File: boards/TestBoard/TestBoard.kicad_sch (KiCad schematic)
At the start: 19 parts, among them J1 Conn_01x04, J2 Conn_01x04, J3 Conn_01x80, J4 Conn_01x13, U1 MCP23017_ML, U2 MCP23017_ML, U3 MCP23017_ML, U4 MCP23017_ML, U5 MCP23017_ML

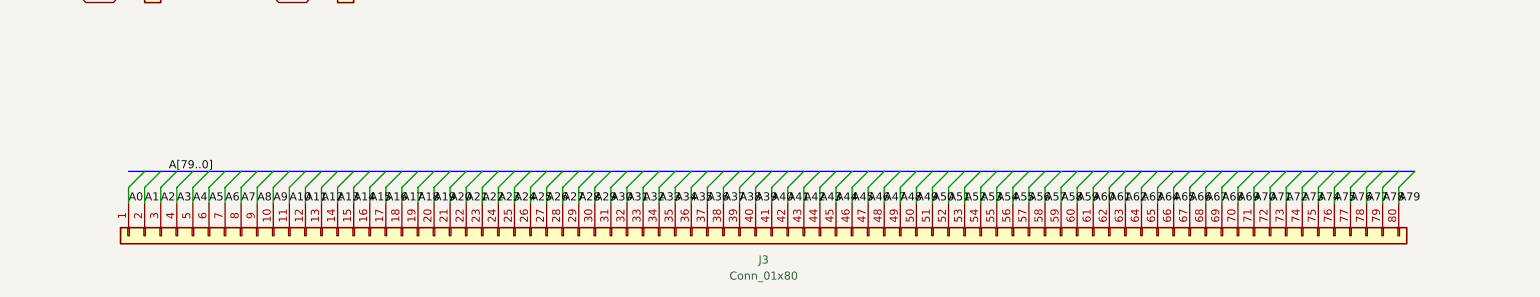
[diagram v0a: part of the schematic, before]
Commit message: Pass-through connectors. Partial manual routing.
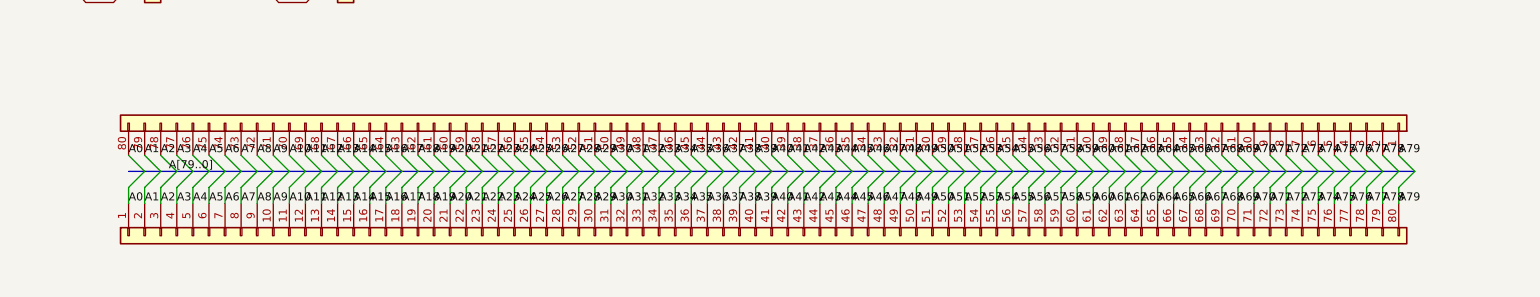
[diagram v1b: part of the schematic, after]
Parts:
- added J5: Conn_01x80, Connector_FFC-FPC:FPC-SMD_THD0518-80CL-GF, symbol Connectors:Conn_01x80
- J4: footprint Connector_PinHeader_2.54mm:PinHeader_1x11_P2.54mm_Vertical -> Connector_PinHeader_2.54mm:PinHeader_1x13_P2.54mm_Vertical
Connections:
- net A0: now also J5.80 (Pin_80)
- net A1: now also J5.79 (Pin_79)
- net A10: now also J5.70 (Pin_70)
- net A11: now also J5.69 (Pin_69)
- net A12: now also J5.68 (Pin_68)
- net A13: now also J5.67 (Pin_67)
- net A14: now also J5.66 (Pin_66)
- net A15: now also J5.65 (Pin_65)
- net A16: now also J5.64 (Pin_64)
- net A17: now also J5.63 (Pin_63)
- net A18: now also J5.62 (Pin_62)
- net A19: now also J5.61 (Pin_61)
- net A2: now also J5.78 (Pin_78)
- net A20: now also J5.60 (Pin_60)
- net A21: now also J5.59 (Pin_59)
- net A22: now also J5.58 (Pin_58)
- net A23: now also J5.57 (Pin_57)
- net A24: now also J5.56 (Pin_56)
- net A25: now also J5.55 (Pin_55)
- net A26: now also J5.54 (Pin_54)
- net A27: now also J5.53 (Pin_53)
- net A28: now also J5.52 (Pin_52)
- net A29: now also J5.51 (Pin_51)
- net A3: now also J5.77 (Pin_77)
- net A30: now also J5.50 (Pin_50)
- net A31: now also J5.49 (Pin_49)
- net A32: now also J5.48 (Pin_48)
- net A33: now also J5.47 (Pin_47)
- net A34: now also J5.46 (Pin_46)
- net A35: now also J5.45 (Pin_45)
- net A36: now also J5.44 (Pin_44)
- net A37: now also J5.43 (Pin_43)
- net A38: now also J5.42 (Pin_42)
- net A39: now also J5.41 (Pin_41)
- net A4: now also J5.76 (Pin_76)
- net A40: now also J5.40 (Pin_40)
- net A41: now also J5.39 (Pin_39)
- net A42: now also J5.38 (Pin_38)
- net A43: now also J5.37 (Pin_37)
- net A44: now also J5.36 (Pin_36)
- net A45: now also J5.35 (Pin_35)
- net A46: now also J5.34 (Pin_34)
- net A47: now also J5.33 (Pin_33)
- net A48: now also J5.32 (Pin_32)
- net A49: now also J5.31 (Pin_31)
- net A5: now also J5.75 (Pin_75)
- net A50: now also J5.30 (Pin_30)
- net A51: now also J5.29 (Pin_29)
- net A52: now also J5.28 (Pin_28)
- net A53: now also J5.27 (Pin_27)
- net A54: now also J5.26 (Pin_26)
- net A55: now also J5.25 (Pin_25)
- net A56: now also J5.24 (Pin_24)
- net A57: now also J5.23 (Pin_23)
- net A58: now also J5.22 (Pin_22)
- net A59: now also J5.21 (Pin_21)
- net A6: now also J5.74 (Pin_74)
- net A60: now also J5.20 (Pin_20)
- net A61: now also J5.19 (Pin_19)
- net A62: now also J5.18 (Pin_18)
- net A63: now also J5.17 (Pin_17)
- net A64: now also J5.16 (Pin_16)
- net A65: now also J5.15 (Pin_15)
- net A66: now also J5.14 (Pin_14)
- net A67: now also J5.13 (Pin_13)
- net A68: now also J5.12 (Pin_12)
- net A69: now also J5.11 (Pin_11)
- net A7: now also J5.73 (Pin_73)
- net A70: now also J5.10 (Pin_10)
- net A71: now also J5.9 (Pin_9)
- net A72: now also J5.8 (Pin_8)
- net A73: now also J5.7 (Pin_7)
- net A74: now also J5.6 (Pin_6)
- net A75: now also J5.5 (Pin_5)
- net A76: now also J5.4 (Pin_4)
- net A77: now also J5.3 (Pin_3)
- net A78: now also J5.2 (Pin_2)
- net A79: now also J5.1 (Pin_1)
- net A8: now also J5.72 (Pin_72)
- net A9: now also J5.71 (Pin_71)

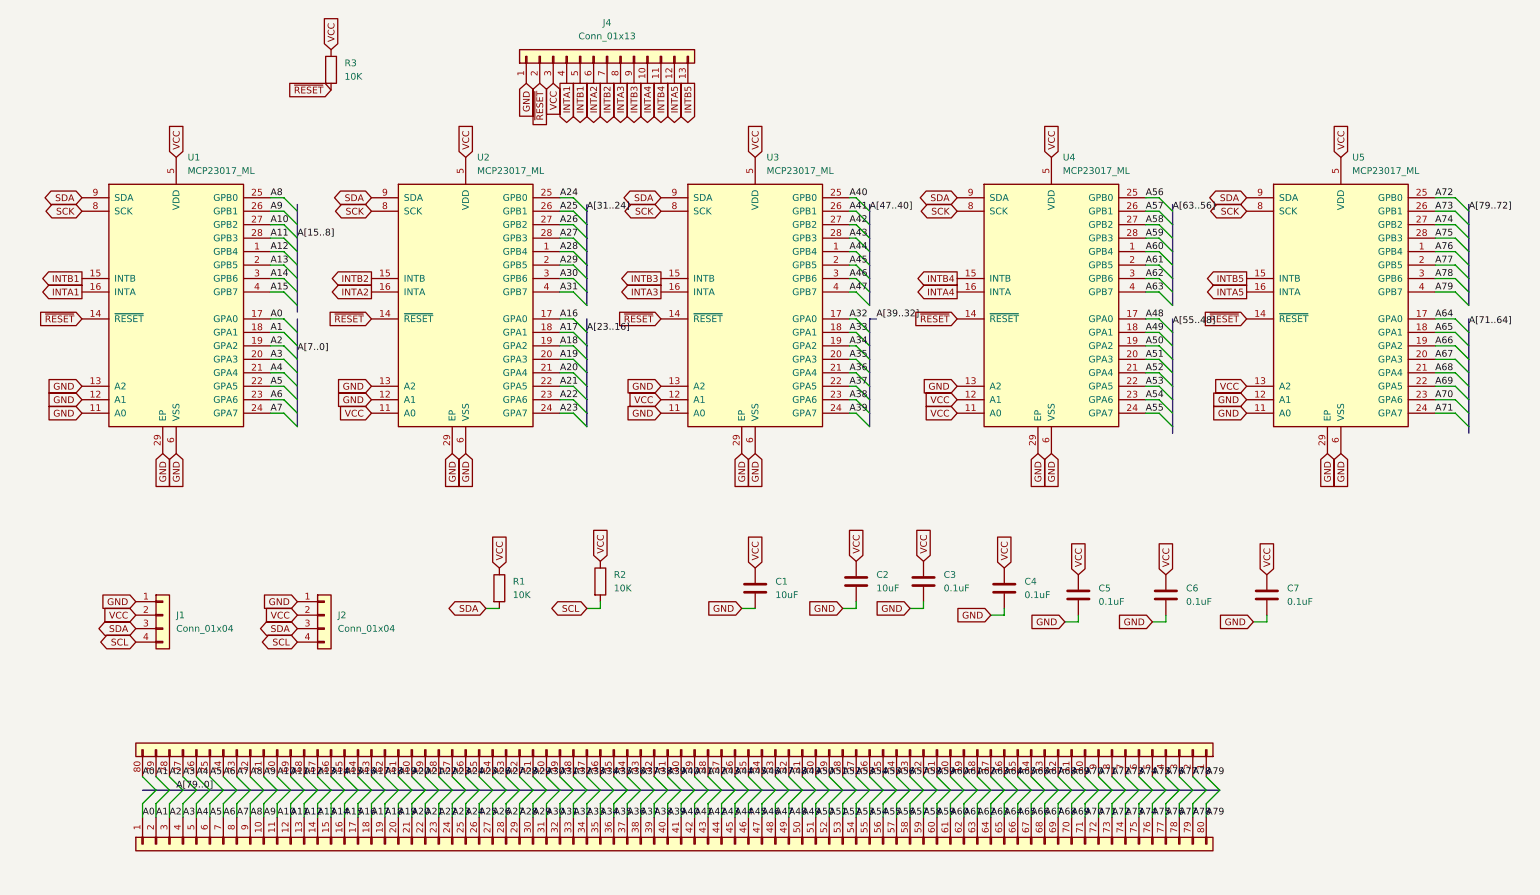
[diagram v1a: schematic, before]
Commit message: Yes: complete auto-routing; "stick" form factor. Silk screen complete.
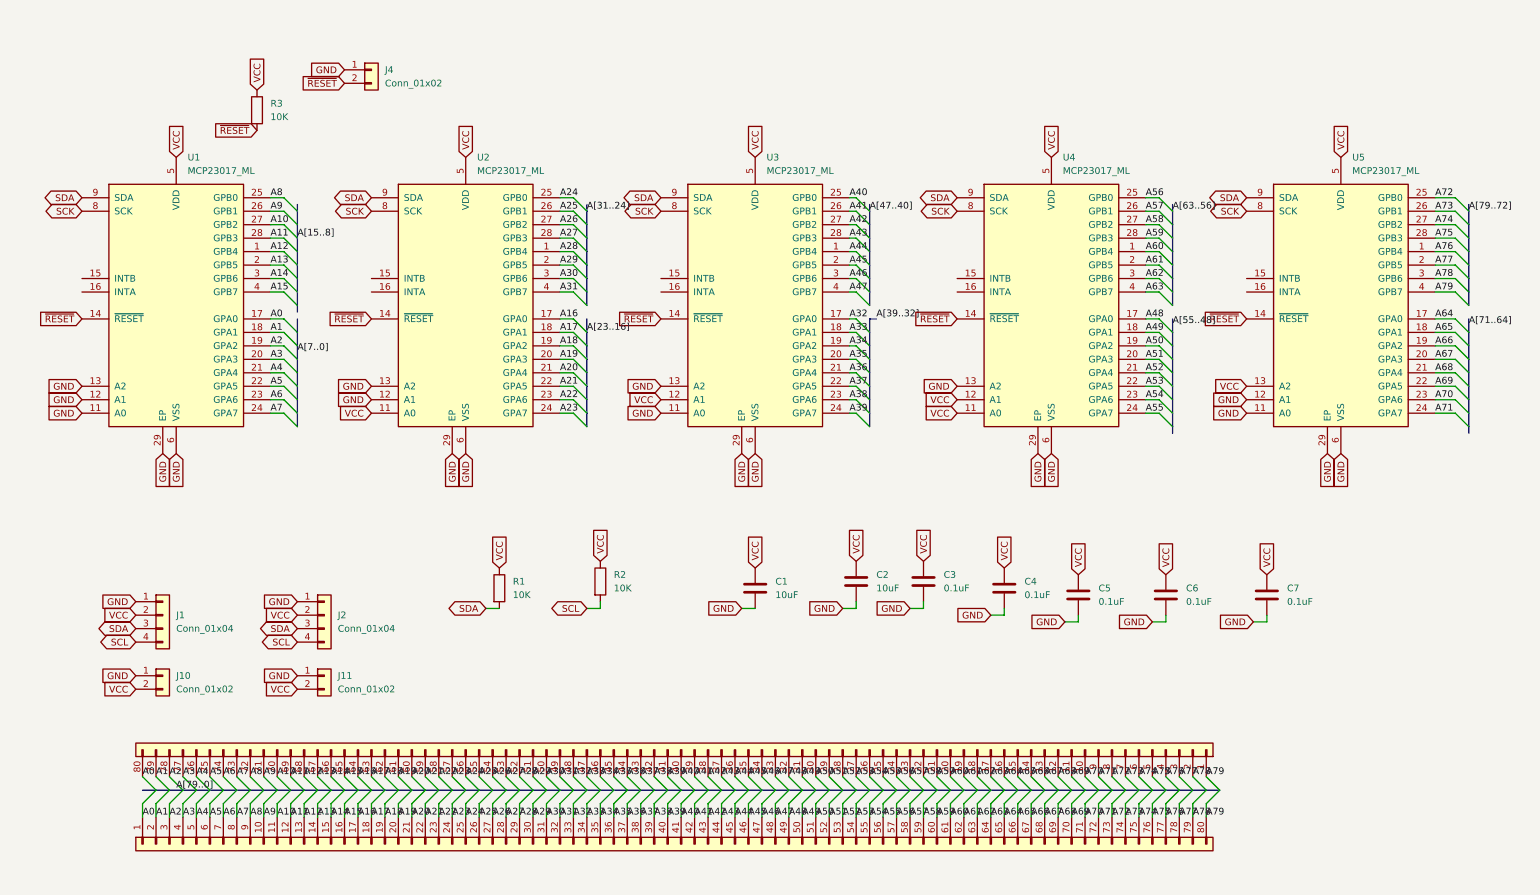
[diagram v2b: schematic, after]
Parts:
- removed J4: Conn_01x13, Connector_PinHeader_2.54mm:PinHeader_1x13_P2.54mm_Vertical, symbol Connector_Generic:Conn_01x13
- added J10, J11, J4: Conn_01x02, Connector_PinHeader_2.54mm:PinHeader_1x02_P2.54mm_Vertical, symbol Connector_Generic:Conn_01x02
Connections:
- net GND: now also J10.1 (Pin_1), J11.1 (Pin_1), J4.1 (Pin_1)
- net VCC: now also J10.2 (Pin_2), J11.2 (Pin_2)
- net ~{RESET}: now also J4.2 (Pin_2)
- net INTA1: no longer names the net of U1.16 (INTA)
- net INTA2: no longer names the net of U2.16 (INTA)
- net INTA3: no longer names the net of U3.16 (INTA)
- net INTA4: no longer names the net of U4.16 (INTA)
- net INTA5: no longer names the net of U5.16 (INTA)
- net INTB1: no longer names the net of U1.15 (INTB)
- net INTB2: no longer names the net of U2.15 (INTB)
- net INTB3: no longer names the net of U3.15 (INTB)
- net INTB4: no longer names the net of U4.15 (INTB)
- net INTB5: no longer names the net of U5.15 (INTB)
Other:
- moved on the sheet: R3

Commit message: Complete BOM LCSC references. Add a board reference.
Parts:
- J1, J2: LCSC (none) -> C160404
- J10, J11, J4: now left out of the parts list
- J3, J5: LCSC (none) -> C283193
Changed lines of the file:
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@@
 		(unit 1)
 		(exclude_from_sim no)
-		(in_bom yes)
+		(in_bom no)
 		(on_board yes)
 		(dnp no)
@@
 			)
 		)
-		(property "LCSC" ""
+		(property "LCSC" "C283193"
 			(at 156.21 147.32 90)
 			(effects
@@
 			)
 		)
-		(property "LCSC" ""
+		(property "LCSC" "C160404"
 			(at 63.5 121.92 0)
 			(effects
@@
 		(unit 1)
 		(exclude_from_sim no)
-		(in_bom yes)
+		(in_bom no)
 		(on_board yes)
 		(dnp no)
@@
 			)
 		)
-		(property "LCSC" ""
+		(property "LCSC" "C283193"
 			(at 102.87 165.1 90)
 			(effects
@@
 			)
 		)
-		(property "LCSC" ""
+		(property "LCSC" "C160404"
 			(at 33.02 121.92 0)
 			(effects
@@
 		(unit 1)
 		(exclude_from_sim no)
-		(in_bom yes)
+		(in_bom no)
 		(on_board yes)
 		(dnp no)

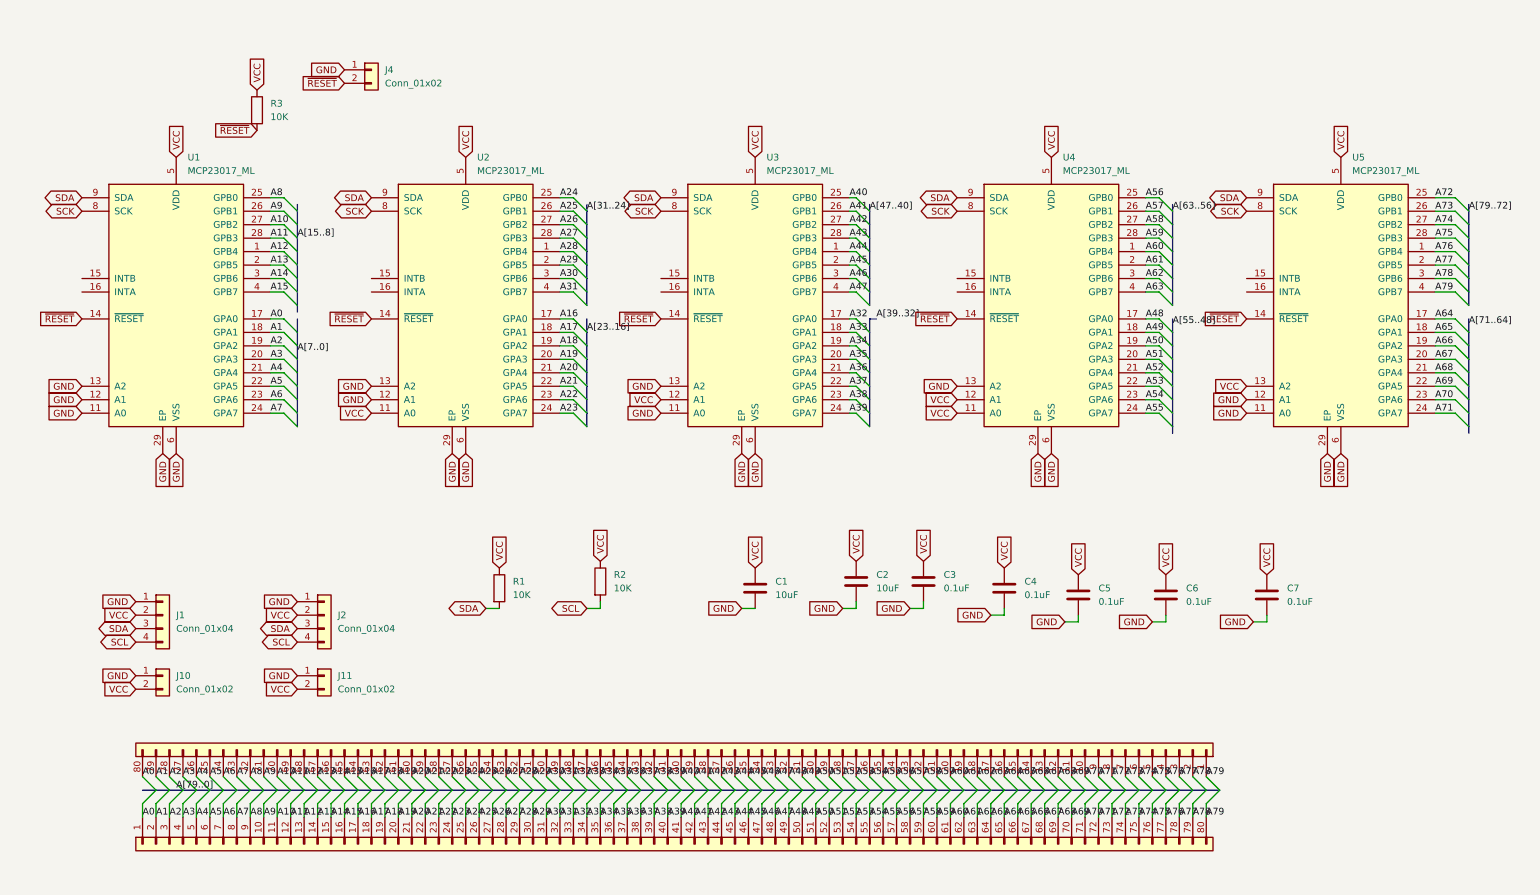
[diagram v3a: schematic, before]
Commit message: Manual routing and SSOP. Only routed the signal lines. Beautiful, isn't it ?
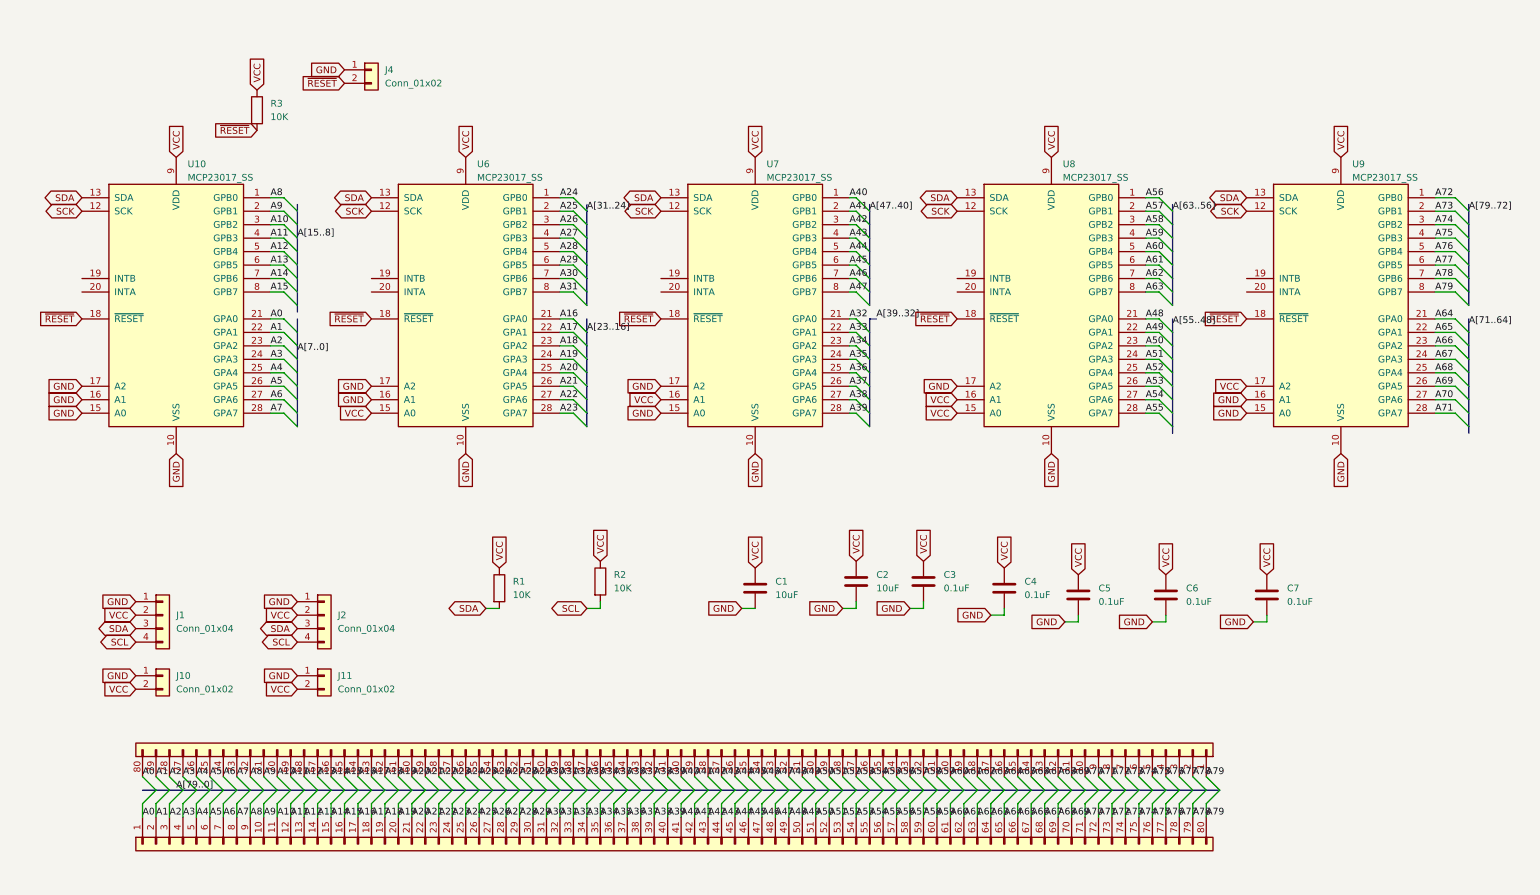
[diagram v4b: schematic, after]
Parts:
- removed U1, U2, U3, U4, U5: MCP23017_ML, Package_DFN_QFN:QFN-28-1EP_6x6mm_P0.65mm_EP4.25x4.25mm, symbol Interface_Expansion:MCP23017_ML
- added U10, U6, U7, U8, U9: MCP23017_SS, Package_SO:SSOP-28_5.3x10.2mm_P0.65mm, symbol Interface_Expansion:MCP23017_SS
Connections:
- net A0: now also U10.21 (GPA0)
- net A1: now also U10.22 (GPA1)
- net A10: now also U10.3 (GPB2)
- net A11: now also U10.4 (GPB3)
- net A12: now also U10.5 (GPB4)
- net A13: now also U10.6 (GPB5)
- net A14: now also U10.7 (GPB6)
- net A15: now also U10.8 (GPB7)
- net A16: now also U6.21 (GPA0)
- net A17: now also U6.22 (GPA1)
- net A18: now also U6.23 (GPA2)
- net A19: now also U6.24 (GPA3)
- net A2: now also U10.23 (GPA2)
- net A20: now also U6.25 (GPA4)
- net A21: now also U6.26 (GPA5)
- net A22: now also U6.27 (GPA6)
- net A23: now also U6.28 (GPA7)
- net A24: now also U6.1 (GPB0)
- net A25: now also U6.2 (GPB1)
- net A26: now also U6.3 (GPB2)
- net A27: now also U6.4 (GPB3)
- net A28: now also U6.5 (GPB4)
- net A29: now also U6.6 (GPB5)
- net A3: now also U10.24 (GPA3)
- net A30: now also U6.7 (GPB6)
- net A31: now also U6.8 (GPB7)
- net A32: now also U7.21 (GPA0)
- net A33: now also U7.22 (GPA1)
- net A34: now also U7.23 (GPA2)
- net A35: now also U7.24 (GPA3)
- net A36: now also U7.25 (GPA4)
- net A37: now also U7.26 (GPA5)
- net A38: now also U7.27 (GPA6)
- net A39: now also U7.28 (GPA7)
- net A4: now also U10.25 (GPA4)
- net A40: now also U7.1 (GPB0)
- net A41: now also U7.2 (GPB1)
- net A42: now also U7.3 (GPB2)
- net A43: now also U7.4 (GPB3)
- net A44: now also U7.5 (GPB4)
- net A45: now also U7.6 (GPB5)
- net A46: now also U7.7 (GPB6)
- net A47: now also U7.8 (GPB7)
- net A48: now also U8.21 (GPA0)
- net A49: now also U8.22 (GPA1)
- net A5: now also U10.26 (GPA5)
- net A50: now also U8.23 (GPA2)
- net A51: now also U8.24 (GPA3)
- net A52: now also U8.25 (GPA4)
- net A53: now also U8.26 (GPA5)
- net A54: now also U8.27 (GPA6)
- net A55: now also U8.28 (GPA7)
- net A56: now also U8.1 (GPB0)
- net A57: now also U8.2 (GPB1)
- net A58: now also U8.3 (GPB2)
- net A59: now also U8.4 (GPB3)
- net A6: now also U10.27 (GPA6)
- net A60: now also U8.5 (GPB4)
- net A61: now also U8.6 (GPB5)
- net A62: now also U8.7 (GPB6)
- net A63: now also U8.8 (GPB7)
- net A64: now also U9.21 (GPA0)
- net A65: now also U9.22 (GPA1)
- net A66: now also U9.23 (GPA2)
- net A67: now also U9.24 (GPA3)
- net A68: now also U9.25 (GPA4)
- net A69: now also U9.26 (GPA5)
- net A7: now also U10.28 (GPA7)
- net A70: now also U9.27 (GPA6)
- net A71: now also U9.28 (GPA7)
- net A72: now also U9.1 (GPB0)
- net A73: now also U9.2 (GPB1)
- net A74: now also U9.3 (GPB2)
- net A75: now also U9.4 (GPB3)
- net A76: now also U9.5 (GPB4)
- net A77: now also U9.6 (GPB5)
- net A78: now also U9.7 (GPB6)
- net A79: now also U9.8 (GPB7)
- net A8: now also U10.1 (GPB0)
- net A9: now also U10.2 (GPB1)
- net GND: now also U10.10 (VSS), U10.15 (A0), U10.16 (A1), U10.17 (A2), U6.10 (VSS), U6.16 (A1), U6.17 (A2), U7.10 (VSS), U7.15 (A0), U7.17 (A2), U8.10 (VSS), U8.17 (A2), U9.10 (VSS), U9.15 (A0), U9.16 (A1)
- net SCK: now also U10.12 (SCK), U6.12 (SCK), U7.12 (SCK), U8.12 (SCK), U9.12 (SCK)
- net SDA: now also U10.13 (SDA), U6.13 (SDA), U7.13 (SDA), U8.13 (SDA), U9.13 (SDA)
- net VCC: now also U10.9 (VDD), U6.15 (A0), U6.9 (VDD), U7.16 (A1), U7.9 (VDD), U8.15 (A0), U8.16 (A1), U8.9 (VDD), U9.17 (A2), U9.9 (VDD)
- net ~{RESET}: now also U10.18 (~{RESET}), U6.18 (~{RESET}), U7.18 (~{RESET}), U8.18 (~{RESET}), U9.18 (~{RESET})
